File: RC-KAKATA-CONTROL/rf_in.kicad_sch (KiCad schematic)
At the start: 4 parts, among them J15 Conn_01x12_Socket

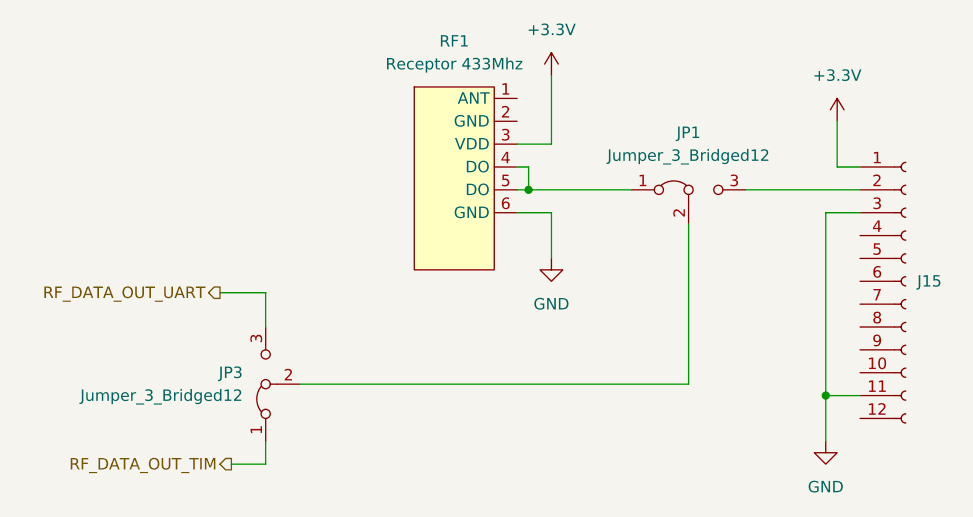
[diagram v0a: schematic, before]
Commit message: Agregadas conexiones de analogicos Agregadas las conexiones de i2c Agregadas las conexiones de Uart Cambiados algunos detalles de tvs resistencias y cap Recolocados los componenetes de power supply Cambiados los diodos de entrada de la bateria por unos de 5A Cambios menores y mejorada la documentacion Agregada informacion en la serigrafia del PCB
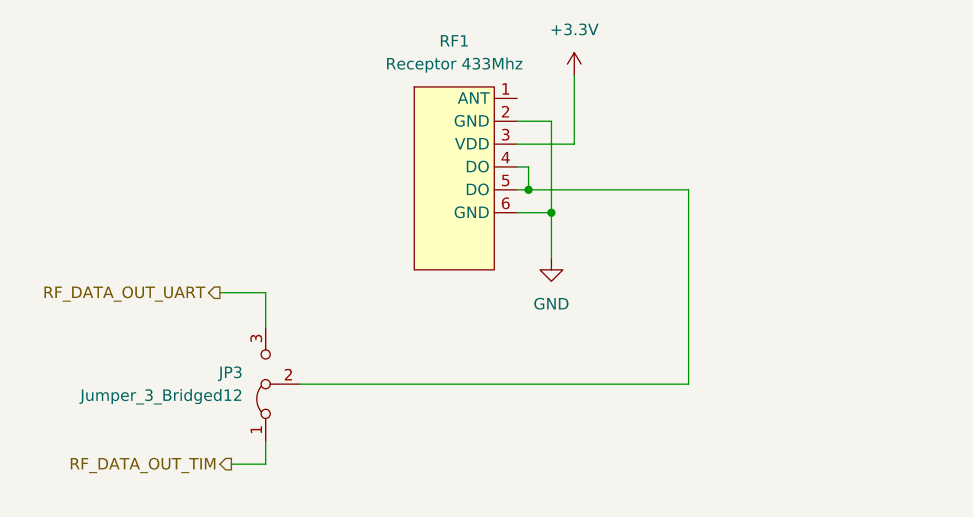
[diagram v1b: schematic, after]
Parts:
- removed J15: Conn_01x12_Socket, Connector_PinSocket_2.54mm:PinSocket_1x12_P2.54mm_Vertical, symbol Connector:Conn_01x12_Socket
- removed JP1: Jumper_3_Bridged12, Connector_PinHeader_2.54mm:PinHeader_1x03_P2.54mm_Vertical, symbol Jumper:Jumper_3_Bridged12
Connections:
- net GND: now also RF1.2 (GND)
- net at RF1.4 (DO), RF1.5 (DO): now also JP3.2 (C)

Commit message: Colocadas todas las piezas Verificacion de conexiones de los puertos UART - I2C - SPI Realizadas todas las conexiones Verificados los errores
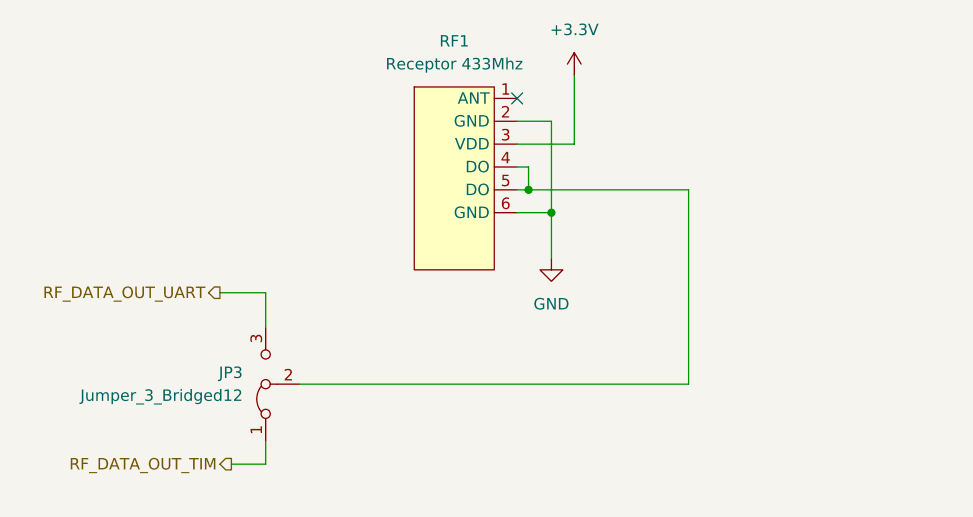
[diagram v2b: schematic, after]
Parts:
- RF1: footprint EasyEDA:Itla_RC_rf_433mhz_receiver -> LOCAL_LIB:rf_433mhz_receiver
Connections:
- no-connect marks 0 -> 1
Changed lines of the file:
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@@
 	(generator "eeschema")
 	(generator_version "9.0")
-	(paper "A4")
+	(paper "USLedger")
 	(title_block
 		(title "RC-KAKATA-CONTROL")
@@
 		(diameter 0)
 		(color 0 0 0 0)
+	)
+	(no_connect
+		(at 121.92 90.17)
 	)
 	(wire
@@
 			)
 		)
-		(property "Footprint" "EasyEDA:Itla_RC_rf_433mhz_receiver"
+		(property "Footprint" "LOCAL_LIB:rf_433mhz_receiver"
 			(at 119.38 88.9 0)
 			(effects
